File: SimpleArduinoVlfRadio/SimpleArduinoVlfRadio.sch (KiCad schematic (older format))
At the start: 14 parts, among them J1 Batt Conn, SW1 SW_Push, U1 L7805, U2 ATmega328P-PU

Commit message: Add Transmitter without off switch
Add the main transmitter circuit. Still need to add the ditigal switch to prevent transmitter and receiver from using same antenna.
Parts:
- gave numbers to parts that had none: 1
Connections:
- wire segments 95 -> 96
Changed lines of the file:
@@
 	7050 4450 7050 4750
 $Comp
-L Custom_Library:FTDI J?
+L Custom_Library:FTDI J2
 U 1 1 5EA9CFE4
 P 7250 4600
-F 0 "J?" H 7478 4251 50  0000 L CNN
+F 0 "J2" H 7478 4251 50  0000 L CNN
 F 1 "FTDI" H 7478 4160 50  0000 L CNN
 F 2 "" H 7250 4550 50  0001 C CNN
@@
 	9050 5650 7900 5650
 Connection ~ 7900 5650
+$Comp
+L power:GND #PWR?
+U 1 1 5EB6A7FF
+P 6950 5800
+F 0 "#PWR?" H 6950 5550 50  0001 C CNN
+F 1 "GND" H 6955 5627 50  0000 C CNN
+F 2 "" H 6950 5800 50  0001 C CNN
+F 3 "" H 6950 5800 50  0001 C CNN
+	1    6950 5800
+	1    0    0    -1
+$EndComp
+Wire Wire Line
+	6950 5800 6950 5650
 $EndSCHEMATC

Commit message: Updated schematic and readme
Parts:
- removed C3, C4: 22pF, symbol Device:C
- removed C5: 0.1uF, symbol Device:C
- removed CP1: 100uF, symbol Device:CP1
- removed CP2: 47uF, symbol Device:CP1
- removed D1: LED, symbol Device:LED
- removed J1: Batt Conn, Connector_JST:JST_XH_B2B-XH-AM_1x02_P2.50mm_Vertical, symbol Connector_Generic:Conn_01x02
- removed J2: FTDI, symbol Custom_Library:FTDI
- removed R1, R2: 10k, symbol Device:R
- removed SW1: SW_Push, symbol Switch:SW_Push
- removed U1: L7805, symbol Regulator_Linear:L7805
- removed U2: ATmega328P-PU, Package_DIP:DIP-28_W7.62mm, symbol MCU_Microchip_ATmega:ATmega328P-PU
- removed Y?: Crystal, symbol Device:Crystal
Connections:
- net labels added: +12V, DigitalSignal
- net labels removed: +BATT, GND
- wire segments 96 -> 5

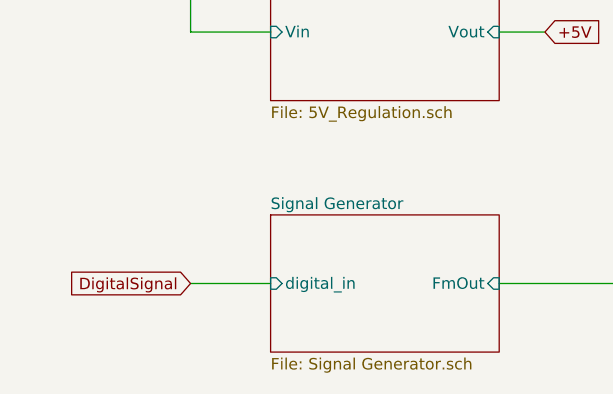
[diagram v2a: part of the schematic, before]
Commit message: Updated functional diagram for 555 enable
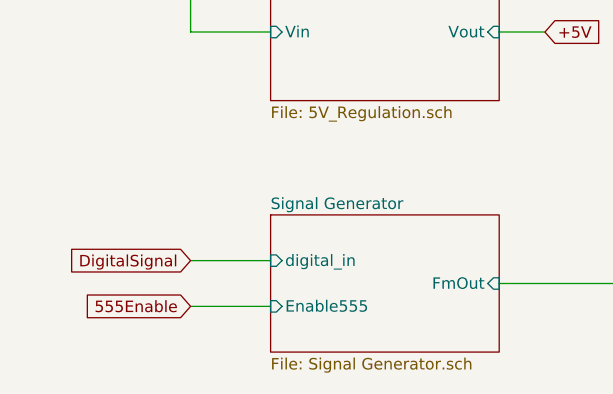
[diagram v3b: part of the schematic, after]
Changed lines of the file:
@@
 $EndDescr
 Wire Wire Line
-	1100 3100 1450 3100
-Text GLabel 1100 3100 0    50   Input ~ 0
+	1100 3000 1450 3000
+Text GLabel 1100 3000 0    50   Input ~ 0
 DigitalSignal
 Wire Wire Line
@@
 F0 "Signal Generator" 50
 F1 "Signal Generator.sch" 50
-F2 "digital_in" I L 1450 3100 50
+F2 "digital_in" I L 1450 3000 50
 F3 "FmOut" I R 2450 3100 50
+F4 "Enable555" I L 1450 3200 50
 $EndSheet
 Text GLabel 2650 2000 2    50   Input ~ 0
@@
 Wire Wire Line
 	2450 3100 3050 3100
+Text GLabel 1100 3200 0    50   Input ~ 0
+555Enable
+Wire Wire Line
+	1100 3200 1450 3200
 $EndSCHEMATC

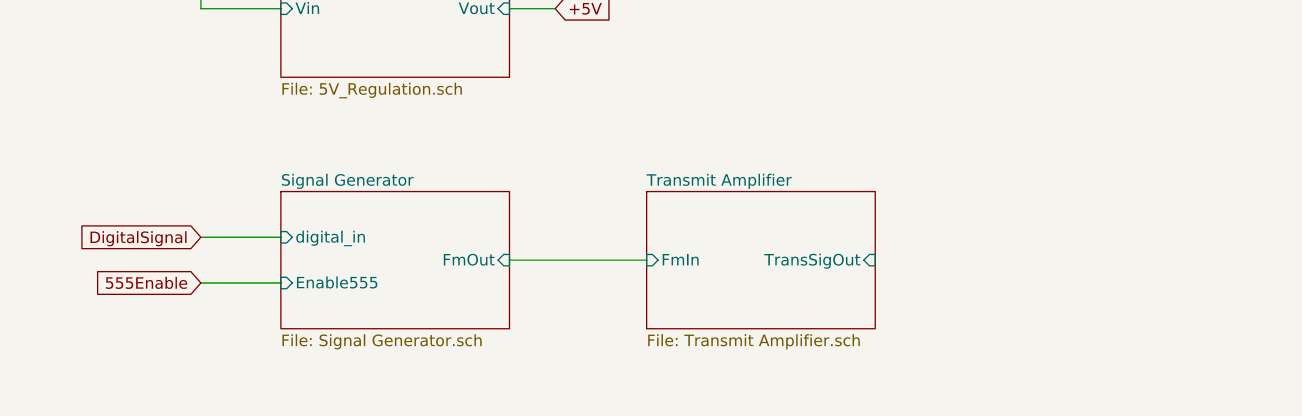
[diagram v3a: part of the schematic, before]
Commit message: Update to working but inefficient design
Design is working well. Need big caps on power for filter and bigger cap for amp. Also need to make sure gain of 10x or more on lm1875. Current draw of 250mA on transmit. Power of 17mA with amplifier disconnected.
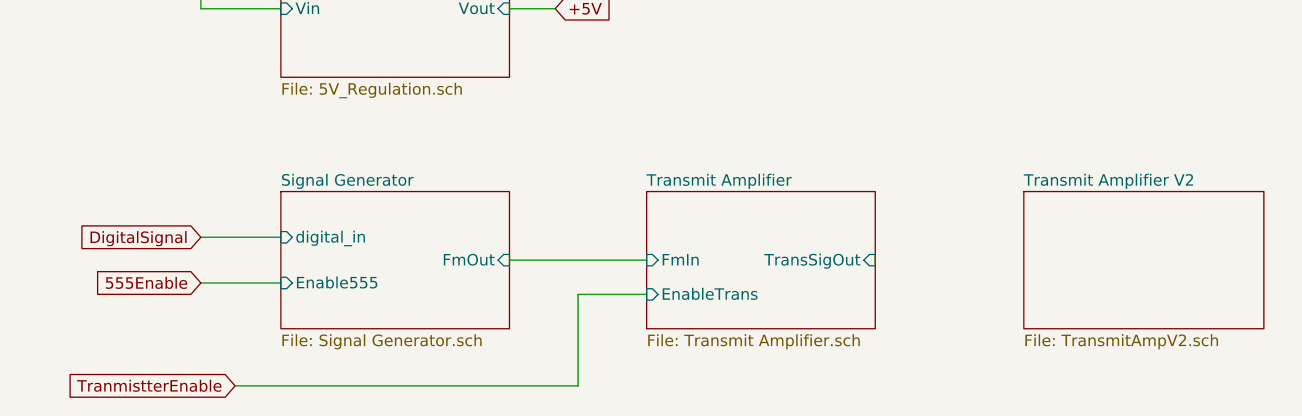
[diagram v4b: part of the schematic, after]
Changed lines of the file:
@@
 $Descr A4 11693 8268
 encoding utf-8
-Sheet 1 4
+Sheet 1 5
 Title "VLF Transmitter"
 Date ""
@@
 F2 "FmIn" I L 3050 3100 50
 F3 "TransSigOut" I R 4050 3100 50
+F4 "EnableTrans" I L 3050 3250 50
 $EndSheet
 Wire Wire Line
@@
 Wire Wire Line
 	1100 3200 1450 3200
+Text GLabel 1250 3650 0    50   Input ~ 0
+TranmistterEnable
+Wire Wire Line
+	1250 3650 2750 3650
+Wire Wire Line
+	2750 3650 2750 3250
+Wire Wire Line
+	2750 3250 3050 3250
+$Sheet
+S 4700 2800 1050 600
+U 61DDCE18
+F0 "Transmit Amplifier V2" 50
+F1 "TransmitAmpV2.sch" 50
+$EndSheet
 $EndSCHEMATC

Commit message: Updates to overall layout.
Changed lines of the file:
@@
 $Descr A4 11693 8268
 encoding utf-8
-Sheet 1 5
+Sheet 1 10
 Title "VLF Transmitter"
 Date ""
@@
 $EndDescr
 Wire Wire Line
-	1100 3000 1450 3000
-Text GLabel 1100 3000 0    50   Input ~ 0
+	1650 3050 2000 3050
+Text GLabel 1650 3050 0    50   Input ~ 0
 DigitalSignal
 Wire Wire Line
-	2650 2000 2450 2000
+	3200 2050 3000 2050
 Wire Wire Line
-	1100 2000 1450 2000
+	1650 2050 2000 2050
 Wire Wire Line
-	1100 1850 1100 2000
+	1650 1900 1650 2050
 $Sheet
-S 1450 2800 1000 600
+S 2000 2850 1000 600
 U 616EB94F
 F0 "Signal Generator" 50
 F1 "Signal Generator.sch" 50
-F2 "digital_in" I L 1450 3000 50
-F3 "FmOut" I R 2450 3100 50
-F4 "Enable555" I L 1450 3200 50
+F2 "digital_in" I L 2000 3050 50
+F3 "FmOut" I R 3000 3150 50
+F4 "Enable555" I L 2000 3250 50
 $EndSheet
-Text GLabel 2650 2000 2    50   Input ~ 0
+Text GLabel 3200 2050 2    50   Input ~ 0
 +5V
 $Comp
 L power:+12V #PWR?
 U 1 1 617092F1
-P 1100 1850
-F 0 "#PWR?" H 1100 1700 50  0001 C CNN
-F 1 "+12V" H 1115 2023 50  0000 C CNN
-F 2 "" H 1100 1850 50  0001 C CNN
-F 3 "" H 1100 1850 50  0001 C CNN
-	1    1100 1850
+P 1650 1900
+F 0 "#PWR?" H 1650 1750 50  0001 C CNN
+F 1 "+12V" H 1665 2073 50  0000 C CNN
+F 2 "" H 1650 1900 50  0001 C CNN
+F 3 "" H 1650 1900 50  0001 C CNN
+	1    1650 1900
 	1    0    0    -1
 $EndComp
 $Sheet
-S 1450 1700 1000 600
+S 2000 1750 1000 600
 U 616E26A8
 F0 "5V_Regulation" 50
 F1 "5V_Regulation.sch" 50
-F2 "Vout" I R 2450 2000 50
-F3 "Vin" I L 1450 2000 50
-$EndSheet
-$Sheet
-S 3050 2800 1000 600
-U 617F980A
-F0 "Transmit Amplifier" 50
-F1 "Transmit Amplifier.sch" 50
-F2 "FmIn" I L 3050 3100 50
-F3 "TransSigOut" I R 4050 3100 50
-F4 "EnableTrans" I L 3050 3250 50
+F2 "Vout" I R 3000 2050 50
+F3 "Vin" I L 2000 2050 50
 $EndSheet
 Wire Wire Line
-	2450 3100 3050 3100
-Text GLabel 1100 3200 0    50   Input ~ 0
+	3000 3150 3600 3150
+Text GLabel 1650 3250 0    50   Input ~ 0
 555Enable
 Wire Wire Line
-	1100 3200 1450 3200
-Text GLabel 1250 3650 0    50   Input ~ 0
+	1650 3250 2000 3250
+Text GLabel 1800 3700 0    50   Input ~ 0
 TranmistterEnable
 Wire Wire Line
-	1250 3650 2750 3650
+	1800 3700 3300 3700
 Wire Wire Line
-	2750 3650 2750 3250
+	3300 3700 3300 3300
 Wire Wire Line
-	2750 3250 3050 3250
+	3300 3300 3600 3300
 $Sheet
-S 4700 2800 1050 600
+S 3600 2850 1050 600
 U 61DDCE18
 F0 "Transmit Amplifier V2" 50
 F1 "TransmitAmpV2.sch" 50
+F2 "FmIn" I L 3600 3150 50
+F3 "TransSigOut" I R 4650 3150 50
+F4 "EnableTrans" I L 3600 3300 50
+$EndSheet
+$Sheet
+S 2000 4100 1050 550
+U 61E50876
+F0 "FSK Decoder" 50
+F1 "fsk_decoder.sch" 50
+$EndSheet
+$Sheet
+S 2000 5000 1050 550
+U 61E508EC
+F0 "Headphone Amp" 50
+F1 "headphone_amp.sch" 50
+$EndSheet
+$Sheet
+S 7800 4100 1050 550
+U 61E503C9
+F0 "Input Stage" 50
+F1 "input_stage.sch" 50
+$EndSheet
+$Sheet
+S 6450 4100 1000 550
+U 61E5142A
+F0 "Interstage Filter" 50
+F1 "interstage_filter.sch" 50
+$EndSheet
+$Sheet
+S 5000 4100 1100 550
+U 61E514ED
+F0 "First Audio Amp" 50
+F1 "first_audio_amp.sch" 50
+$EndSheet
+$Sheet
+S 3600 4100 1050 550
+U 61E504B6
+F0 "Second Amp and Filter" 50
+F1 "second_amp_filter.sch" 50
+$EndSheet
+$Sheet
+S 9350 3300 1150 600
+U 61E52474
+F0 "Antenna" 50
+F1 "Antenna.sch" 50
 $EndSheet
 $EndSCHEMATC

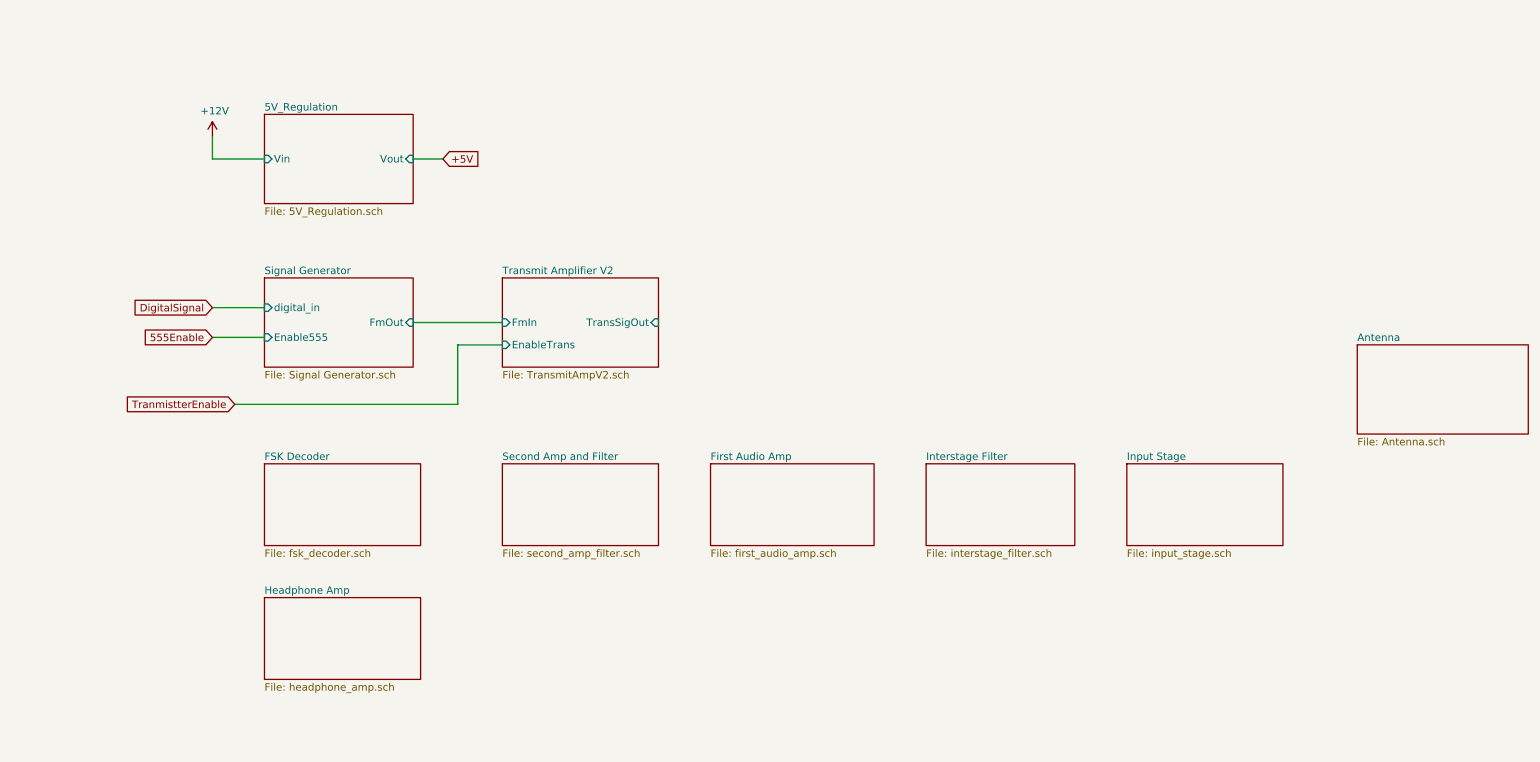
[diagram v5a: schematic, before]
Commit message: Updated Transmitter and finished fsk receiver
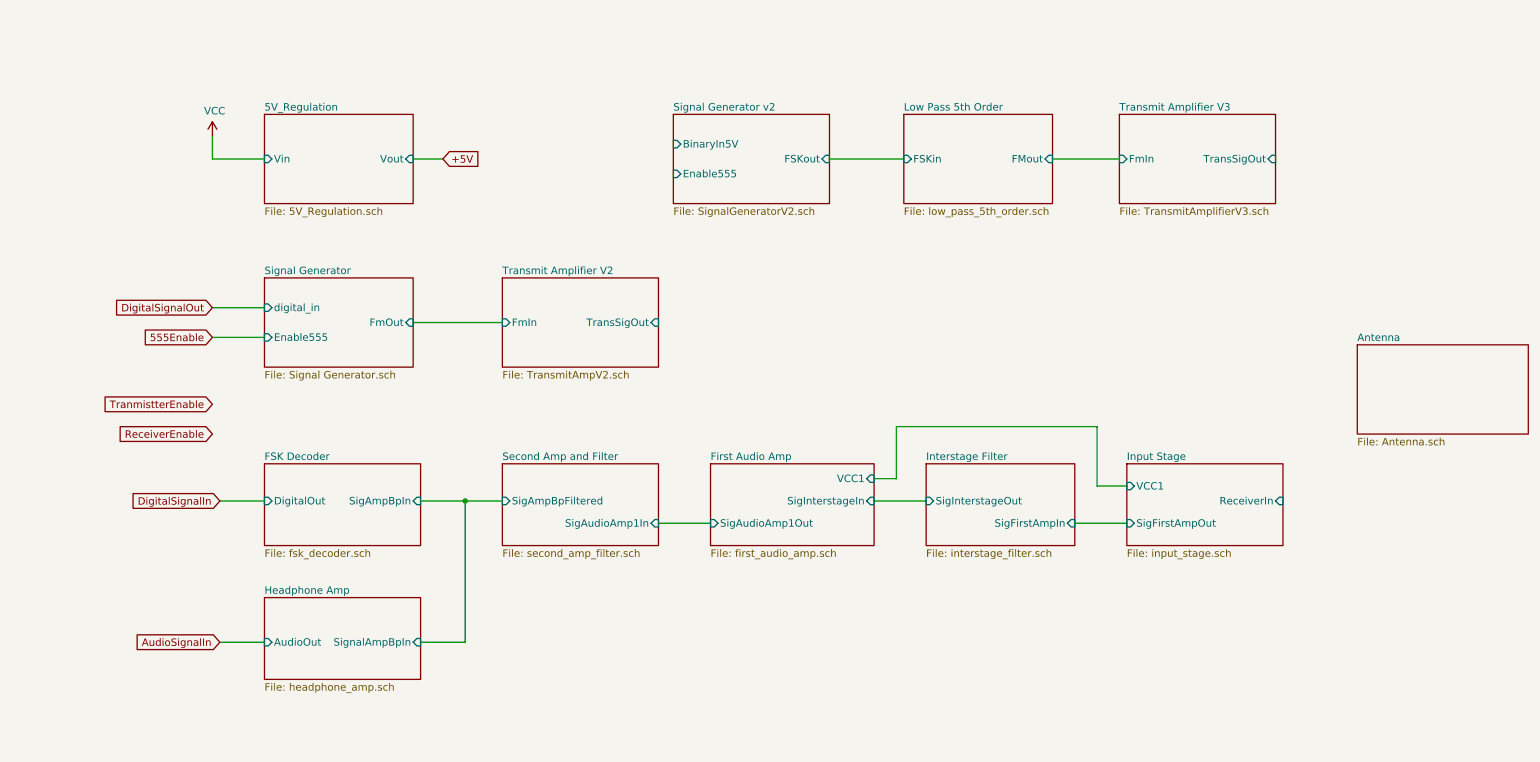
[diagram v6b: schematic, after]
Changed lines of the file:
@@
 $Descr A4 11693 8268
 encoding utf-8
-Sheet 1 10
+Sheet 1 14
 Title "VLF Transmitter"
 Date ""
@@
 	1650 3050 2000 3050
 Text GLabel 1650 3050 0    50   Input ~ 0
-DigitalSignal
+DigitalSignalOut
 Wire Wire Line
 	3200 2050 3000 2050
@@
 Text GLabel 3200 2050 2    50   Input ~ 0
 +5V
-$Comp
-L power:+12V #PWR?
-U 1 1 617092F1
-P 1650 1900
-F 0 "#PWR?" H 1650 1750 50  0001 C CNN
-F 1 "+12V" H 1665 2073 50  0000 C CNN
-F 2 "" H 1650 1900 50  0001 C CNN
-F 3 "" H 1650 1900 50  0001 C CNN
-	1    1650 1900
-	1    0    0    -1
-$EndComp
 $Sheet
 S 2000 1750 1000 600
@@
 Wire Wire Line
 	1650 3250 2000 3250
-Text GLabel 1800 3700 0    50   Input ~ 0
+Text GLabel 1650 3700 0    50   Input ~ 0
 TranmistterEnable
-Wire Wire Line
-	1800 3700 3300 3700
-Wire Wire Line
-	3300 3700 3300 3300
-Wire Wire Line
-	3300 3300 3600 3300
 $Sheet
 S 3600 2850 1050 600
@@
 F2 "FmIn" I L 3600 3150 50
 F3 "TransSigOut" I R 4650 3150 50
-F4 "EnableTrans" I L 3600 3300 50
 $EndSheet
 $Sheet
@@
 F0 "FSK Decoder" 50
 F1 "fsk_decoder.sch" 50
+F2 "SigAmpBpIn" I R 3050 4350 50
+F3 "DigitalOut" I L 2000 4350 50
 $EndSheet
 $Sheet
@@
 F0 "Headphone Amp" 50
 F1 "headphone_amp.sch" 50
+F2 "SignalAmpBpIn" I R 3050 5300 50
+F3 "AudioOut" I L 2000 5300 50
 $EndSheet
 $Sheet
@@
 F0 "Input Stage" 50
 F1 "input_stage.sch" 50
-$EndSheet
-$Sheet
-S 6450 4100 1000 550
-U 61E5142A
-F0 "Interstage Filter" 50
-F1 "interstage_filter.sch" 50
+F2 "ReceiverIn" I R 8850 4350 50
+F3 "SigFirstAmpOut" I L 7800 4500 50
+F4 "VCC1" I L 7800 4250 50
 $EndSheet
 $Sheet
@@
 F0 "First Audio Amp" 50
 F1 "first_audio_amp.sch" 50
+F2 "VCC1" I R 6100 4200 50
+F3 "SigInterstageIn" I R 6100 4350 50
+F4 "SigAudioAmp1Out" I L 5000 4500 50
 $EndSheet
 $Sheet
@@
 F0 "Second Amp and Filter" 50
 F1 "second_amp_filter.sch" 50
+F2 "SigAudioAmp1In" I R 4650 4500 50
+F3 "SigAmpBpFiltered" I L 3600 4350 50
 $EndSheet
 $Sheet
@@
 F1 "Antenna.sch" 50
 $EndSheet
+$Sheet
+S 6450 4100 1000 550
+U 61E5142A
+F0 "Interstage Filter" 50
+F1 "interstage_filter.sch" 50
+F2 "SigFirstAmpIn" I R 7450 4500 50
+F3 "SigInterstageOut" I L 6450 4350 50
+$EndSheet
+Wire Wire Line
+	7800 4250 7600 4250
+Wire Wire Line
+	7600 4250 7600 3850
+Wire Wire Line
+	7600 3850 6250 3850
+Wire Wire Line
+	6250 3850 6250 4200
+Wire Wire Line
+	6250 4200 6100 4200
+Wire Wire Line
+	7450 4500 7800 4500
+Wire Wire Line
+	6450 4350 6100 4350
+Text GLabel 1700 4350 0    50   Input ~ 0
+DigitalSignalIn
+Wire Wire Line
+	2000 4350 1700 4350
+Text GLabel 1650 3900 0    50   Input ~ 0
+ReceiverEnable
+Text GLabel 1700 5300 0    50   Input ~ 0
+AudioSignalIn
+Wire Wire Line
+	2000 5300 1700 5300
+Wire Wire Line
+	3600 4350 3350 4350
+Wire Wire Line
+	3350 4350 3350 5300
+Wire Wire Line
+	3350 5300 3050 5300
+Connection ~ 3350 4350
+Wire Wire Line
+	3350 4350 3050 4350
+$Sheet
+S 4750 1750 1050 600
+U 62C385F2
+F0 "Signal Generator v2" 50
+F1 "SignalGeneratorV2.sch" 50
+F2 "FSKout" I R 5800 2050 50
+F3 "BinaryIn5V" I L 4750 1950 50
+F4 "Enable555" I L 4750 2150 50
+$EndSheet
+$Sheet
+S 6300 1750 1000 600
+U 62C578A0
+F0 "Low Pass 5th Order" 50
+F1 "low_pass_5th_order.sch" 50
+F2 "FSKin" I L 6300 2050 50
+F3 "FMout" I R 7300 2050 50
+$EndSheet
+$Sheet
+S 7750 1750 1050 600
+U 62C5F7EE
+F0 "Transmit Amplifier V3" 50
+F1 "TransmitAmplifierV3.sch" 50
+F2 "FmIn" I L 7750 2050 50
+F3 "TransSigOut" I R 8800 2050 50
+$EndSheet
+Wire Wire Line
+	5000 4500 4650 4500
+Wire Wire Line
+	5800 2050 6300 2050
+Wire Wire Line
+	7300 2050 7750 2050
+$Comp
+L power:VCC #PWR?
+U 1 1 62C7D911
+P 1650 1900
+F 0 "#PWR?" H 1650 1750 50  0001 C CNN
+F 1 "VCC" H 1665 2073 50  0000 C CNN
+F 2 "" H 1650 1900 50  0001 C CNN
+F 3 "" H 1650 1900 50  0001 C CNN
+	1    1650 1900
+	1    0    0    -1
+$EndComp
 $EndSCHEMATC
